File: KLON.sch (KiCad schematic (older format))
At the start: 69 parts, among them IC1 MAX1044ESA+, J1 Conn_01x03, J2 Conn_01x03, J3 Conn_01x02, SW1 3PDT, U1 TL072, U2 TL072

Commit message: updates. Going to temporarily remove ground connections in PCB file to make it easier to route.
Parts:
- IC1: footprint SOIC127P600X175-8N -> Housings_DIP:DIP-8_W7.62mm_Socket
- Z1: footprint DIOAD1413W86L463D238 -> projectfootprints:DIODEAD1413W86L463D238
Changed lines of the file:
@@
 LIBS:contrib
 LIBS:valves
-LIBS:dk_USB-DVI-HDMI-Connectors
-LIBS:dk_TVS-Mixed-Technology
-LIBS:dk_TVS-Diodes
-LIBS:dk_Trimmer-Potentiometers
-LIBS:dk_Transistors-JFETs
-LIBS:dk_Transistors-FETs-MOSFETs-Single
-LIBS:dk_Transistors-FETs-MOSFETs-RF
-LIBS:dk_Transistors-FETs-MOSFETs-Arrays
-LIBS:dk_Transistors-Bipolar-BJT-Single
-LIBS:dk_Transistors-Bipolar-BJT-Single-Pre-Biased
-LIBS:dk_Transistors-Bipolar-BJT-RF
-LIBS:dk_Transistors-Bipolar-BJT-Arrays
-LIBS:dk_Toggle-Switches
-LIBS:dk_Thyristors-TRIACs
-LIBS:dk_Thyristors-SCRs
-LIBS:dk_Thyristors-DIACs-SIDACs
-LIBS:dk_Thermal-Cutoffs-Thermal-Fuses
-LIBS:dk_Temperature-Sensors-Analog-and-Digital-Output
-LIBS:dk_Tactile-Switches
-LIBS:dk_Surge-Suppression-ICs
-LIBS:dk_Specialized-Sensors
-LIBS:dk_Specialized-ICs
-LIBS:dk_Solid-State-Relays
-LIBS:dk_Slide-Switches
-LIBS:dk_Signal-Relays-Up-to-2-Amps
-LIBS:dk_Sensors-Transducers_Accessories
-LIBS:dk_Rotary-Potentiometers-Rheostats
-LIBS:dk_RFID-RF-Access-Monitoring-ICs
-LIBS:dk_RF-Transmitters
-LIBS:dk_RF-Transceiver-Modules
-LIBS:dk_RF-Transceiver-ICs
-LIBS:dk_RF-Switches
-LIBS:dk_RF-Receivers
-LIBS:dk_RF-Evaluation-and-Development-Kits-Boards
-LIBS:dk_RF-Detectors
-LIBS:dk_RF-Demodulators
-LIBS:dk_RF-Antennas
-LIBS:dk_RF-Amplifiers
-LIBS:dk_Resistor-Networks-Arrays
-LIBS:dk_Reed-Relays
-LIBS:dk_Rectangular-Connectors-Headers-Male-Pins
-LIBS:dk_Pushbutton-Switches
-LIBS:dk_Programmable-Oscillators
-LIBS:dk_Pressure-Sensors-Transducers
-LIBS:dk_Power-Relays-Over-2-Amps
-LIBS:dk_PMIC-Voltage-Regulators-Special-Purpose
-LIBS:dk_PMIC-Voltage-Regulators-Linear
-LIBS:dk_PMIC-Voltage-Regulators-DC-DC-Switching-Regulators
-LIBS:dk_PMIC-Voltage-Regulators-DC-DC-Switching-Controllers
-LIBS:dk_PMIC-Voltage-Reference
-LIBS:dk_PMIC-V-F-and-F-V-Converters
-LIBS:dk_PMIC-Thermal-Management
-LIBS:dk_PMIC-Supervisors
-LIBS:dk_PMIC-RMS-to-DC-Converters
-LIBS:dk_PMIC-Power-Management-Specialized
-LIBS:dk_PMIC-Power-Distribution-Switches-Load-Drivers
-LIBS:dk_PMIC-OR-Controllers-Ideal-Diodes
-LIBS:dk_PMIC-Motor-Drivers-Controllers
-LIBS:dk_PMIC-LED-Drivers
-LIBS:dk_PMIC-Gate-Drivers
-LIBS:dk_PMIC-Full-Half-Bridge-Drivers
-LIBS:dk_PMIC-Current-Regulation-Management
-LIBS:dk_PMIC-Battery-Management
-LIBS:dk_PMIC-Battery-Chargers
-LIBS:dk_PMIC-AC-DC-Converters-Offline-Switchers
-LIBS:dk_Oscillators
-LIBS:dk_Optoisolators-Triac-SCR-Output
-LIBS:dk_Optoisolators-Transistor-Photovoltaic-Output
-LIBS:dk_Optoisolators-Logic-Output
-LIBS:dk_Optical-Sensors-Reflective-Analog-Output
-LIBS:dk_Optical-Sensors-Phototransistors
-LIBS:dk_Optical-Sensors-Photodiodes
-LIBS:dk_Optical-Sensors-Photo-Detectors-Remote-Receiver
-LIBS:dk_Optical-Sensors-Ambient-Light-IR-UV-Sensors
-LIBS:dk_Navigation-Switches-Joystick
-LIBS:dk_Motion-Sensors-Tilt-Switches
-LIBS:dk_Motion-Sensors-IMUs-Inertial-Measurement-Units
-LIBS:dk_Motion-Sensors-Accelerometers
-LIBS:dk_Modular-Connectors-Jacks
-LIBS:dk_Modular-Connectors-Jacks-With-Magnetics
-LIBS:dk_Microphones
-LIBS:dk_Memory
-LIBS:dk_Memory-Connectors-PC-Card-Sockets
-LIBS:dk_Magnetic-Sensors-Switches-Solid-State
-LIBS:dk_Magnetic-Sensors-Linear-Compass-ICs
-LIBS:dk_Magnetic-Sensors-Compass-Magnetic-Field-Modules
-LIBS:dk_Logic-Translators-Level-Shifters
-LIBS:dk_Logic-Signal-Switches-Multiplexers-Decoders
-LIBS:dk_Logic-Shift-Registers
-LIBS:dk_Logic-Multivibrators
-LIBS:dk_Logic-Gates-and-Inverters
-LIBS:dk_Logic-Flip-Flops
-LIBS:dk_Logic-Buffers-Drivers-Receivers-Transceivers
-LIBS:dk_Linear-Comparators
-LIBS:dk_Linear-Amplifiers-Instrumentation-OP-Amps-Buffer-Amps
-LIBS:dk_Linear-Amplifiers-Audio
-LIBS:dk_LEDs-Circuit-Board-Indicators-Arrays-Light-Bars-Bar-Graphs
-LIBS:dk_LED-Indication-Discrete
-LIBS:dk_Interface-Specialized
-LIBS:dk_Interface-Sensor-Capacitive-Touch
-LIBS:dk_Interface-Sensor-and-Detector-Interfaces
-LIBS:dk_Interface-Modules
-LIBS:dk_Interface-I-O-Expanders
-LIBS:dk_Interface-Drivers-Receivers-Transceivers
-LIBS:dk_Interface-Controllers
-LIBS:dk_Interface-Analog-Switches-Special-Purpose
-LIBS:dk_Interface-Analog-Switches-Multiplexers-Demultiplexers
-LIBS:dk_Inrush-Current-Limiters-ICL
-LIBS:dk_Infrared-UV-Visible-Emitters
-LIBS:dk_Image-Sensors-Camera
-LIBS:dk_Humidity-Moisture-Sensors
-LIBS:dk_Gas-Sensors
-LIBS:dk_Fuses
-LIBS:dk_Fixed-Inductors
-LIBS:dk_Ferrite-Beads-and-Chips
-LIBS:dk_Evaluation-Boards-Sensors
-LIBS:dk_Encoders
-LIBS:dk_Embedded-Microcontrollers
-LIBS:dk_Display-Modules-LED-Character-and-Numeric
-LIBS:dk_Diodes-Zener-Single
-LIBS:dk_Diodes-Rectifiers-Single
-LIBS:dk_Diodes-Rectifiers-Arrays
-LIBS:dk_Diodes-Bridge-Rectifiers
-LIBS:dk_Digital-Isolators
-LIBS:dk_DC-DC-Converters
-LIBS:dk_Data-Acquisition-Touch-Screen-Controllers
-LIBS:dk_Data-Acquisition-Digital-to-Analog-Converters-DAC
-LIBS:dk_Data-Acquisition-Digital-Potentiometers
-LIBS:dk_Data-Acquisition-Analog-to-Digital-Converters-ADC
-LIBS:dk_Data-Acquisition-ADCs-DACs-Special-Purpose
-LIBS:dk_D-Sub-Connectors
-LIBS:dk_Current-Transducers
-LIBS:dk_Coaxial-Connectors-RF
-LIBS:dk_Clock-Timing-Real-Time-Clocks
-LIBS:dk_Clock-Timing-Programmable-Timers-and-Oscillators
-LIBS:dk_Clock-Timing-Clock-Generators-PLLs-Frequency-Synthesizers
-LIBS:dk_Battery-Holders-Clips-Contacts
-LIBS:dk_Barrel-Audio-Connectors
-LIBS:dk_Balun
-LIBS:dk_Automotive-Relays
-LIBS:dk_Alarms-Buzzers-and-Sirens
-LIBS:dk_Addressable-Specialty
 LIBS:3PDT
 LIBS:MAX1044ESA+
@@
 F 0 "IC1" H 9200 2050 50  0000 L CNN
 F 1 "MAX1044ESA+" H 9000 1950 50  0000 L CNN
-F 2 "SOIC127P600X175-8N" H 9650 1900 50  0001 L CNN
+F 2 "Housings_DIP:DIP-8_W7.62mm_Socket" H 9650 1900 50  0001 L CNN
 F 3 "http://datasheets.maximintegrated.com/en/ds/ICL7660-MAX1044.pdf" H 9650 1800 50  0001 L CNN
 F 4 "Charge Pump Switched Cap 20mA 5V" H 9650 1700 50  0001 L CNN "Description"
@@
 F 0 "Z1" H 7950 550 50  0000 L BNN
 F 1 "1N4742ATR" H 7800 900 50  0000 L BNN
-F 2 "DIOAD1413W86L463D238" H 8050 900 50  0001 L BNN
+F 2 "projectfootprints:DIODEAD1413W86L463D238" H 8050 900 50  0001 L BNN
 F 3 "http://uk.rs-online.com/web/p/products/8050075" H 8050 800 50  0001 L BNN
 F 4 "Diode, Fairchild, 1N4742ATR Fairchild 1N4742ATR Zener Diode, 12V 5% 1 W Through Hole 2-Pin DO-41" H 8050 700 50  0001 L BNN "Description"

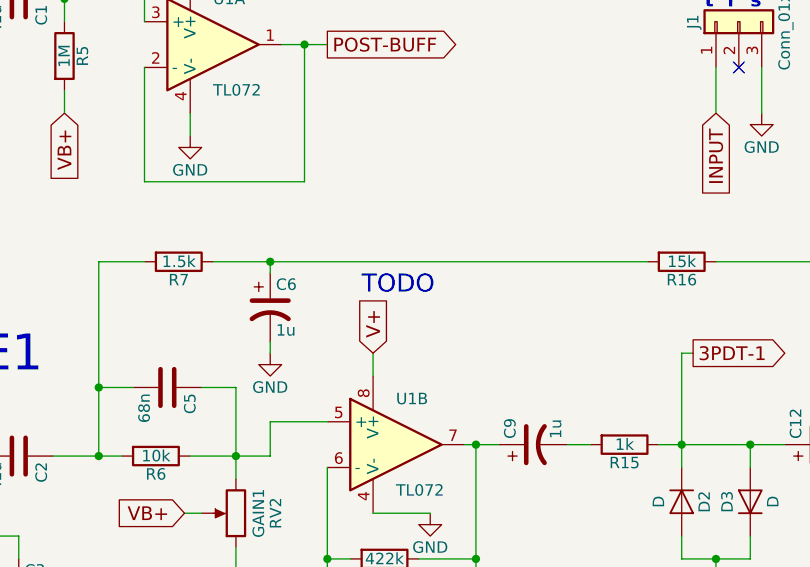
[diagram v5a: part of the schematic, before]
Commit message: Finished .kicad_pcb. Oshpark quote is $45 for 3 boards. Those cuts aren't pretty, but they are cheap.
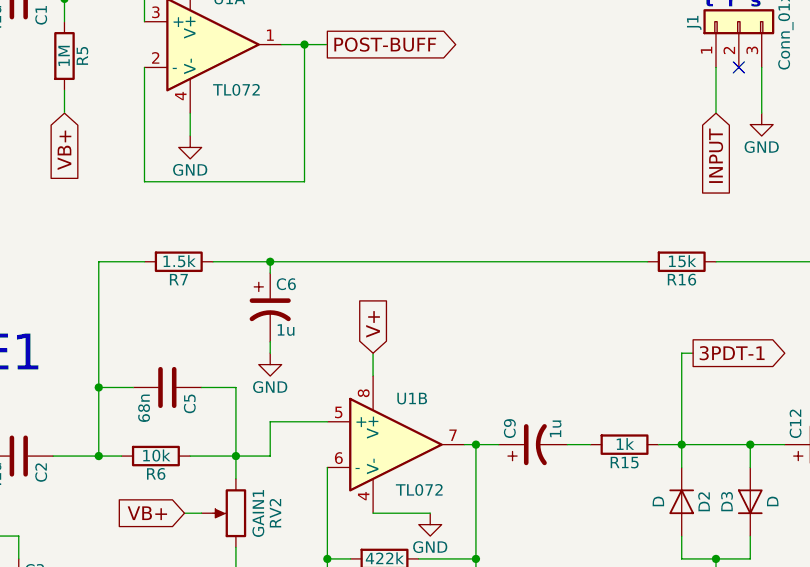
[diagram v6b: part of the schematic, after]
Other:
- note removed: "TODO"
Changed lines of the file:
@@
 	0    1    1    0
 $EndComp
-Text Notes 3200 2000 0    79   ~ 0
-TODO
 $Comp
 L D D2
